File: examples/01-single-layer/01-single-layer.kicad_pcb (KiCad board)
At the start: 2 copper layers, 52.1 x 46.4 mm, 15 parts, among them P1 IN, P2 OUT, P3 POWER, P4 CONN_2, P5 MOUNTING_HOLE, P6 MOUNTING_HOLE, P7 MOUNTING_HOLE, P8 MOUNTING_HOLE, U1 ECC83

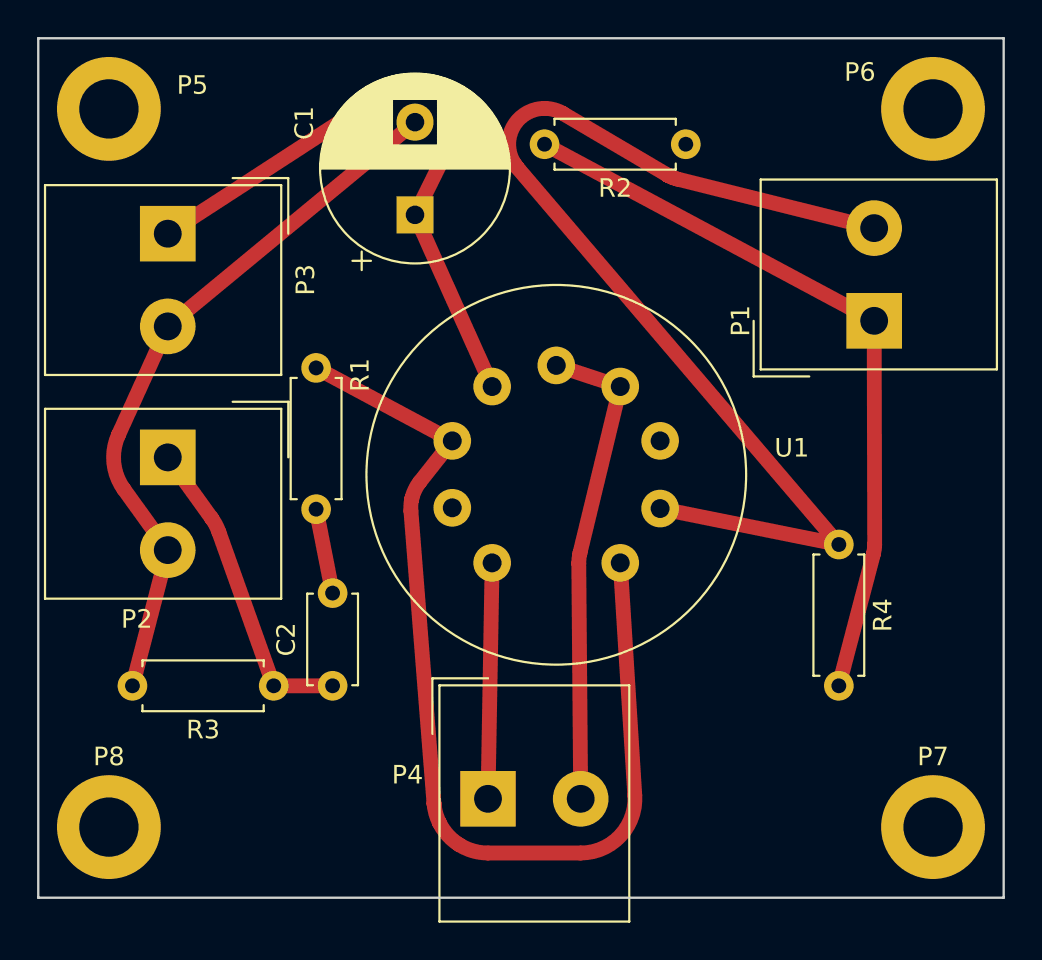
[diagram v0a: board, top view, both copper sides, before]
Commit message: feat(obstacles): convex shapes instead of enclosing circles
An obstacle is now a convex polygon inflated by the clearance radius --
the Minkowski sum of the polygon with a disc. Its boundary is the
polygon's edges pushed outward, joined by arcs on circles centred at its
*vertices*, so the taut path is still lines and arcs. One representation
covers the board: 1 vertex is a disc (round pad, via), 2 a capsule
(track segment, oval pad), 4 a rounded rectangle (rect pad).

The enclosing circle over-covered a long pad by up to sqrt(2) in every
direction -- room the router could not use and connections it refused
that would have fitted. A finished track also cost ~44 chained discs
where it now costs one capsule.

Two real bugs surfaced while testing this on a denser board.

**Pad orientation was 90 degrees out.** The angle in a pad's
(at x y angle) is the pad's *absolute* orientation, not an offset to add
to its footprint's. Adding them is wrong by exactly the footprint angle,
which turns a tall pad into a wide one. Pinned empirically by a property
the boards guarantee -- KiCad reports no overlapping pads on these
demos, so a correct model cannot invent any. Adding the angles invents
26 pad-pad overlaps on sonde xilinx; the pad's own angle invents none.
This one bug accounted for 20 of 23 DRC errors, and it also cost an
hour chasing a solder-mask theory that turned out to be a symptom.

**Copper graphics were not obstacles at all.** Boards carry text drawn
directly on copper layers; it belongs to no net, so copper must clear
it. Missing them was worth a clearance violation apiece.

Also: arcs flatter than 5 um of sagitta are now emitted as their chord.
KiCad rebuilds an arc from three points, and when those are nearly
collinear the reconstruction is ill-conditioned enough that a nanometre
of rounding can flip the sweep -- turning a 12 um sliver into copper
that loops most of the way round a circle.

Results, all judged by kicad-cli:

  ecc83-pp   F.Cu         17/20 -> 19/2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
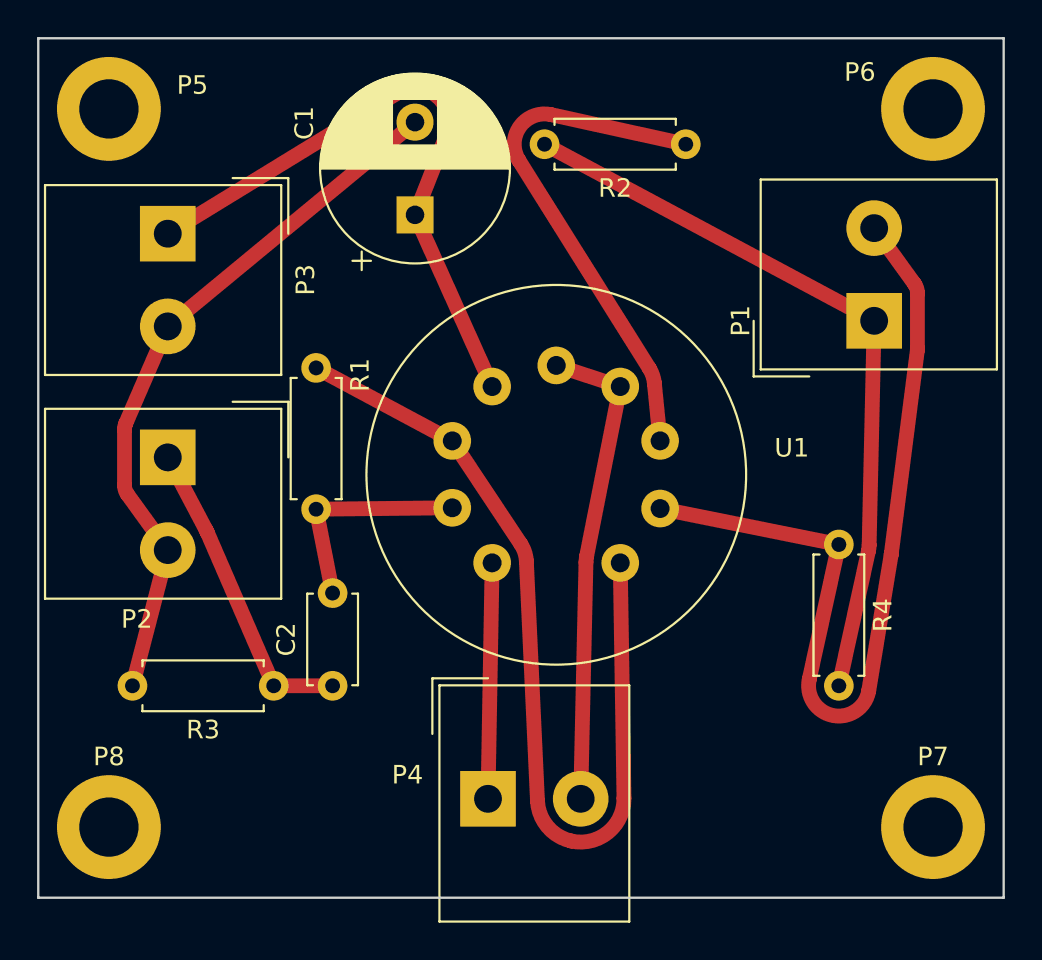
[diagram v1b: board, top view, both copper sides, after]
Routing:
- net Net-(U1B-K): track 0.00 -> 28.3 mm
- net Net-(P1-PM): track 59.9 -> 47.8 mm
- net Net-(U1A-K): track 4.61 -> 12.0 mm
- net Net-(U1A-G): track 55.2 -> 48.7 mm
- net Net-(P3-P1): track 34.5 -> 33.6 mm
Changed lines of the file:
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@@
 	(segment
 		(start 150.542 131.191)
-		(end 150.437649 118.483372)
+		(end 150.826459 118.423814)
 		(width 0.8)
 		(layer "F.Cu")
@@
 	)
 	(arc
-		(start 150.437649 118.483372)
-		(mid 150.45226 118.209056)
-		(end 150.500378 117.938598)
+		(start 150.826459 118.423814)
+		(mid 150.836968 118.263904)
+		(end 150.861284 118.105505)
 		(width 0.8)
 		(layer "F.Cu")
@@
 	)
 	(segment
-		(start 150.500378 117.938598)
+		(start 150.861284 118.105505)
 		(end 152.675 108.955)
 		(width 0.8)
@@
 	(segment
 		(start 166.37 105.41)
-		(end 166.398366 117.470453)
-		(width 0.8)
-		(layer "F.Cu")
-		(net 1)
-	)
-	(arc
-		(start 166.398366 117.470453)
-		(mid 166.382779 117.720047)
-		(end 166.335105 117.965541)
-		(width 0.8)
-		(layer "F.Cu")
-		(net 1)
-	)
-	(segment
-		(start 166.335105 117.965541)
+		(end 166.098589 117.511637)
+		(width 0.8)
+		(layer "F.Cu")
+		(net 1)
+	)
+	(arc
+		(start 166.098589 117.511637)
+		(mid 166.087392 117.669424)
+		(end 166.06099 117.825388)
+		(width 0.8)
+		(layer "F.Cu")
+		(net 1)
+	)
+	(segment
+		(start 166.06099 117.825388)
 		(end 164.465 125.095)
 		(width 0.8)
@@
 	(segment
 		(start 164.465 117.475)
-		(end 147.119066 97.139701)
-		(width 0.8)
-		(layer "F.Cu")
-		(net 5)
-	)
-	(arc
-		(start 147.119066 97.139701)
-		(mid 147.061187 97.068493)
-		(end 147.006753 96.994618)
-		(width 0.8)
-		(layer "F.Cu")
-		(net 5)
-	)
-	(arc
-		(start 147.006753 96.994618)
-		(mid 146.874887 94.992638)
-		(end 148.59 93.951629)
-		(width 0.8)
-		(layer "F.Cu")
-		(net 5)
-	)
-	(arc
-		(start 148.59 93.951629)
-		(mid 149.098437 94.019681)
-		(end 149.571082 94.219047)
-		(width 0.8)
-		(layer "F.Cu")
-		(net 5)
-	)
-	(segment
-		(start 149.571082 94.219047)
-		(end 155.228918 97.550953)
-		(width 0.8)
-		(layer "F.Cu")
-		(net 5)
-	)
-	(arc
-		(start 155.228918 97.550953)
-		(mid 155.229664 97.551393)
-		(end 155.23041 97.551831)
-		(width 0.8)
-		(layer "F.Cu")
-		(net 5)
-	)
-	(arc
-		(start 155.23041 97.551831)
-		(mid 155.234638 97.554309)
-		(end 155.238872 97.556776)
-		(width 0.8)
-		(layer "F.Cu")
-		(net 5)
-	)
-	(arc
-		(start 155.238872 97.556776)
-		(mid 155.244769 97.560187)
-		(end 155.250678 97.563578)
-		(width 0.8)
-		(layer "F.Cu")
-		(net 5)
-	)
-	(arc
-		(start 155.250678 97.563578)
-		(mid 155.355031 97.619056)
-		(end 155.462578 97.668054)
-		(width 0.8)
-		(layer "F.Cu")
-		(net 5)
-	)
-	(arc
-		(start 155.462578 97.668054)
-		(mid 155.600713 97.719855)
-		(end 155.742397 97.760972)
-		(width 0.8)
-		(layer "F.Cu")
-		(net 5)
-	)
-	(segment
-		(start 155.742397 97.760972)
+		(end 162.86901 124.744612)
+		(width 0.8)
+		(layer "F.Cu")
+		(net 5)
+	)
+	(arc
+		(start 162.86901 124.744612)
+		(mid 164.156812 126.699673)
+		(end 166.077241 125.360774)
+		(width 0.8)
+		(layer "F.Cu")
+		(net 5)
+	)
+	(segment
+		(start 166.077241 125.360774)
+		(end 167.286071 118.027751)
+		(width 0.8)
+		(layer "F.Cu")
+		(net 5)
+	)
+	(segment
+		(start 167.286071 118.027751)
+		(end 167.292506 117.983805)
+		(width 0.8)
+		(layer "F.Cu")
+		(net 5)
+	)
+	(segment
+		(start 167.292506 117.983805)
+		(end 168.697243 107.015951)
+		(width 0.8)
+		(layer "F.Cu")
+		(net 5)
+	)
+	(segment
+		(start 168.697243 107.015951)
+		(end 168.704 106.91)
+		(width 0.8)
+		(layer "F.Cu")
+		(net 5)
+	)
+	(segment
+		(start 168.704 106.91)
+		(end 168.704 103.91)
+		(width 0.8)
+		(layer "F.Cu")
+		(net 5)
+	)
+	(arc
+		(start 168.704 103.91)
+		(mid 168.663518 103.653318)
+		(end 168.546001 103.421555)
+		(width 0.8)
+		(layer "F.Cu")
+		(net 5)
+	)
+	(segment
+		(start 168.546001 103.421555)
 		(end 166.37 100.41)
 		(width 0.8)
@@
 	)
 	(segment
+		(start 156.21 95.885)
+		(end 148.940388 94.28901)
+		(width 0.8)
+		(layer "F.Cu")
+		(net 13)
+	)
+	(arc
+		(start 148.940388 94.28901)
+		(mid 147.253886 94.944385)
+		(end 147.205679 96.753108)
+		(width 0.8)
+		(layer "F.Cu")
+		(net 13)
+	)
+	(segment
+		(start 147.205679 96.753108)
+		(end 154.241468 107.972667)
+		(width 0.8)
+		(layer "F.Cu")
+		(net 13)
+	)
+	(arc
+		(start 154.241468 107.972667)
+		(mid 154.424415 108.356379)
+		(end 154.514895 108.771733)
+		(width 0.8)
+		(layer "F.Cu")
+		(net 13)
+	)
+	(segment
+		(start 154.514895 108.771733)
+		(end 154.825 111.885)
+		(width 0.8)
+		(layer "F.Cu")
+		(net 13)
+	)
+	(segment
 		(start 133.985 125.095)
-		(end 131.023338 116.79369)
+		(end 130.411602 116.848046)
 		(width 0.8)
 		(layer "F.Cu")
 		(net 3)
 	)
-	(arc
-		(start 131.023338 116.79369)
-		(mid 130.858121 116.416798)
-		(end 130.641618 116.06684)
+	(segment
+		(start 130.411602 116.848046)
+		(end 130.334103 116.686489)
 		(width 0.8)
 		(layer "F.Cu")
@@
 	)
 	(segment
-		(start 130.641618 116.06684)
+		(start 130.334103 116.686489)
 		(end 128.27 112.776)
 		(width 0.8)
@@
 	(segment
 		(start 141.605 99.695)
-		(end 143.591617 95.677321)
+		(end 143.31117 95.367711)
 		(width 0.8)
 		(layer "F.Cu")
@@
 	)
 	(arc
-		(start 143.591617 95.677321)
-		(mid 143.07807 93.039202)
-		(end 140.398106 92.836235)
+		(start 143.31117 95.367711)
+		(mid 142.784293 93.290428)
+		(end 140.647172 93.130992)
 		(width 0.8)
 		(layer "F.Cu")
@@
 	)
 	(segment
-		(start 140.398106 92.836235)
+		(start 140.647172 93.130992)
 		(end 128.27 100.711)
 		(width 0.8)
@@
 	(segment
 		(start 128.27 105.711)
-		(end 125.60867 111.566403)
-		(width 0.8)
-		(layer "F.Cu")
-		(net 1)
-	)
-	(arc
-		(start 125.60867 111.566403)
-		(mid 125.360975 113.064746)
-		(end 125.898382 114.48516)
-		(width 0.8)
-		(layer "F.Cu")
-		(net 1)
-	)
-	(segment
-		(start 125.898382 114.48516)
+		(end 126.004622 110.944711)
+		(width 0.8)
+		(layer "F.Cu")
+		(net 1)
+	)
+	(arc
+		(start 126.004622 110.944711)
+		(mid 125.953336 111.106839)
+		(end 125.936 111.276)
+		(width 0.8)
+		(layer "F.Cu")
+		(net 1)
+	)
+	(segment
+		(start 125.936 111.276)
+		(end 125.936 114.276)
+		(width 0.8)
+		(layer "F.Cu")
+		(net 1)
+	)
+	(arc
+		(start 125.936 114.276)
+		(mid 125.976482 114.532682)
+		(end 126.093999 114.764445)
+		(width 0.8)
+		(layer "F.Cu")
+		(net 1)
+	)
+	(segment
+		(start 126.093999 114.764445)
 		(end 128.27 117.776)
 		(width 0.8)
@@
 	(segment
 		(start 143.615 111.885)
-		(end 141.859132 114.108275)
-		(width 0.8)
-		(layer "F.Cu")
-		(net 12)
-	)
-	(arc
-		(start 141.859132 114.108275)
-		(mid 141.59624 114.53028)
-		(end 141.433034 114.999923)
-		(width 0.8)
-		(layer "F.Cu")
-		(net 12)
-	)
-	(arc
-		(start 141.433034 114.999923)
-		(mid 141.427095 115.026866)
-		(end 141.421489 115.05388)
-		(width 0.8)
-		(layer "F.Cu")
-		(net 12)
-	)
-	(arc
-		(start 141.421489 115.05388)
-		(mid 141.381578 115.361189)
-		(end 141.384511 115.671065)
-		(width 0.8)
-		(layer "F.Cu")
-		(net 12)
-	)
-	(segment
-		(start 141.384511 115.671065)
-		(end 142.627745 131.421038)
-		(width 0.8)
-		(layer "F.Cu")
-		(net 12)
-	)
-	(arc
-		(start 142.627745 131.421038)
-		(mid 142.630623 131.454978)
-		(end 142.633896 131.488882)
-		(width 0.8)
-		(layer "F.Cu")
-		(net 12)
-	)
-	(arc
-		(start 142.633896 131.488882)
-		(mid 142.731067 131.993781)
-		(end 142.915194 132.473845)
-		(width 0.8)
-		(layer "F.Cu")
-		(net 12)
-	)
-	(arc
-		(start 142.915194 132.473845)
-		(mid 143.367397 133.14469)
-		(end 143.986152 133.665902)
-		(width 0.8)
-		(layer "F.Cu")
-		(net 12)
-	)
-	(arc
-		(start 143.986152 133.665902)
-		(mid 144.73241 133.99998)
-		(end 145.542 134.11432)
-		(width 0.8)
-		(layer "F.Cu")
-		(net 12)
-	)
-	(segment
-		(start 145.542 134.11432)
-		(end 150.542 134.11432)
-		(width 0.8)
-		(layer "F.Cu")
-		(net 12)
-	)
-	(arc
-		(start 150.542 134.11432)
-		(mid 152.672647 133.192536)
-		(end 153.459618 131.008498)
-		(width 0.8)
-		(layer "F.Cu")
-		(net 12)
-	)
-	(segment
-		(start 153.459618 131.008498)
+		(end 147.305307 117.442134)
+		(width 0.8)
+		(layer "F.Cu")
+		(net 12)
+	)
+	(arc
+		(start 147.305307 117.442134)
+		(mid 147.522308 117.88996)
+		(end 147.612019 118.379439)
+		(width 0.8)
+		(layer "F.Cu")
+		(net 12)
+	)
+	(segment
+		(start 147.612019 118.379439)
+		(end 148.2105 131.299003)
+		(width 0.8)
+		(layer "F.Cu")
+		(net 12)
+	)
+	(arc
+		(start 148.2105 131.299003)
+		(mid 148.753309 132.69038)
+		(end 150.02852 133.467817)
+		(width 0.8)
+		(layer "F.Cu")
+		(net 12)
+	)
+	(arc
+		(start 150.02852 133.467817)
+		(mid 152.013952 133.002329)
+		(end 152.875708 131.154087)
+		(width 0.8)
+		(layer "F.Cu")
+		(net 12)
+	)
+	(segment
+		(start 152.875708 131.154087)
 		(end 152.675 118.465)
 		(width 0.8)
@@
 	)
 	(segment
+		(start 136.271 115.57)
+		(end 143.615 115.495)
+		(width 0.8)
+		(layer "F.Cu")
+		(net 4)
+	)
+	(segment
